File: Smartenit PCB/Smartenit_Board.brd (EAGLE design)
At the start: 54.9 x 71.8 mm, 86 parts, among them J1 2X5CONNECTOR1.27MM, Q1 QUARTZ_3.58M_2PIN, U1 SN74LVC1G3157, U2 ADE7953, U3 ESP-WROOM-32

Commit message: fixed diodes
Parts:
- D1: value (none) -> P6SMB16A; device SparkFun:SMA-DIODE -> diode:SMB
- D3: value 250mA/100V -> SS32_DIODE; device diode:DO214BA -> Smart_Charger:D0-214AB
- moved D1 72.2 mm to (-6.22, -78.3), turned to 0 degrees
- moved D3 51.8 mm to (-11.4, -68.6), turned to 0 degrees
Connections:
- net AGND: now also D3.P; no longer D3.A
- net N$18: now also D3.N; no longer D3.C
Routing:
- net N$18: track 14.6 -> 10.8 mm
- net PILOT: track 72.6 -> 69.1 mm
- net DGND: track 104.3 -> 103.6 mm
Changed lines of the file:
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@@
 <attribute name="VALUE" x="47.6154" y="-57.9006" size="0.3048" layer="27" font="vector" ratio="20" align="top-center"/>
-</element>
-<element name="D3" library="diode" library_urn="urn:adsk.eagle:library:210" package="DO214BA" package3d_urn="urn:adsk.eagle:package:43453/2" value="250mA/100V" x="39.156" y="-57.0584" smashed="yes" rot="R90">
-<attribute name="NAME" x="39.3846" y="-59.4206" size="0.6096" layer="25" font="vector" ratio="20" rot="R90" align="bottom-center"/>
 </element>
 <element name="R39" library="SparkFun-Resistors" package="0603" value="100k" x="25.76" y="-68.59" smashed="yes" rot="R180">
@@
 <attribute name="NAME" x="24.977" y="-7.841" size="1.27" layer="25"/>
 <attribute name="VALUE" x="25.231" y="-13.429" size="1.27" layer="27"/>
-</element>
-<element name="D1" library="SparkFun" package="SMA-DIODE" value="" x="13.85" y="-8.96" smashed="yes" rot="R180">
-<attribute name="NAME" x="17.152" y="-10.1284" size="0.4064" layer="25" rot="R180"/>
-<attribute name="VALUE" x="13.596" y="-10.611" size="0.4064" layer="27" rot="R180"/>
 </element>
 <element name="C2" library="SparkFun" package="0603-CAP" value="10uF/6.3V" x="39.973" y="-22.5176" smashed="yes" rot="R270">
@@
 <attribute name="VALUE" x="25.9044" y="-62.7914" size="0.8128" layer="27" rot="R270"/>
 </element>
+<element name="D3" library="Smart_Charger" package="D0-214AB" value="SS32_DIODE" x="-11.3538" y="-68.6308"/>
+<element name="D1" library="diode" library_urn="urn:adsk.eagle:library:210" package="SMB" package3d_urn="urn:adsk.eagle:package:43404/2" value="P6SMB16A" x="-6.223" y="-78.3082"/>
 </elements>
 <signals>
@@
 <signal name="N$18">
 <contactref element="U$4" pad="1"/>
-<contactref element="D3" pad="C"/>
 <contactref element="L1" pad="P$2"/>
 <contactref element="C25" pad="2"/>
-<wire x1="39.0752" y1="-58.975" x2="39.156" y2="-59.1084" width="0.6096" layer="1"/>
 <wire x1="36.3928" y1="-60.3588" x2="35.92" y2="-59.886" width="0.8128" layer="1"/>
 <wire x1="35.92" y1="-59.886" x2="35.92" y2="-58.975" width="0.8128" layer="1"/>
 <wire x1="35.92" y1="-58.975" x2="39.0752" y2="-58.975" width="0.8128" layer="1"/>
-<wire x1="39.156" y1="-59.1084" x2="41.6114" y2="-56.4388" width="0.8128" layer="1"/>
 <wire x1="41.6114" y1="-56.4388" x2="47.3516" y2="-56.4388" width="0.8128" layer="1"/>
 <wire x1="47.3516" y1="-56.4388" x2="47.6154" y2="-56.7026" width="0.8128" layer="1"/>
+<contactref element="D3" pad="N"/>
+<wire x1="35.92" y1="-59.886" x2="-4.5438" y2="-68.6308" width="0" layer="19" extent="1-1"/>
+<wire x1="41.6114" y1="-56.4388" x2="39.0752" y2="-58.975" width="0" layer="19" extent="1-1"/>
 </signal>
 <signal name="N$19">
@@
 <contactref element="R8" pad="2"/>
 <contactref element="R3" pad="2"/>
-<contactref element="D1" pad="C"/>
 <contactref element="U$3" pad="8"/>
 <wire x1="5.015" y1="-13.365" x2="4.4" y2="-13.98" width="0.6096" layer="1"/>
@@
 <wire x1="3.13" y1="-22.76" x2="3.2" y2="-22.83" width="0.4064" layer="16"/>
 <wire x1="5.015" y1="-13.365" x2="9.42" y2="-8.96" width="0.8" layer="1"/>
-<wire x1="9.42" y1="-8.96" x2="11.7" y2="-8.96" width="0.8" layer="1"/>
-<wire x1="11.7" y1="-8.96" x2="12.5906" y2="-8.0694" width="0.8" layer="1"/>
 <wire x1="12.5906" y1="-8.0694" x2="13.97" y2="-6.69" width="0.8" layer="1"/>
 <wire x1="13.97" y1="-6.69" x2="21.69" y2="-6.69" width="0.8" layer="1"/>
@@
 <wire x1="5.56" y1="-48.565" x2="5.56" y2="-53.94" width="0.4064" layer="16"/>
 <wire x1="5.56" y1="-53.94" x2="3.33" y2="-56.17" width="0.4064" layer="16"/>
+<contactref element="D1" pad="C"/>
+<wire x1="3.33" y1="-56.17" x2="-8.423" y2="-78.3082" width="0" layer="19" extent="1-1"/>
+<wire x1="12.5906" y1="-8.0694" x2="9.42" y2="-8.96" width="0" layer="19" extent="1-1"/>
 </signal>
 <signal name="LNV2">
@@
 <contactref element="C24" pad="2"/>
 <contactref element="C23" pad="1"/>
-<contactref element="D3" pad="A"/>
 <contactref element="C6" pad="1"/>
 <contactref element="U$3" pad="7"/>
@@
 <wire x1="11.1506" y1="-7.8994" x2="9.2202" y2="-7.8994" width="0.6096" layer="16"/>
 <via x="9.2202" y="-7.8994" extent="1-16" drill="0.35"/>
+<contactref element="D3" pad="P"/>
+<wire x1="5.33" y1="-56.17" x2="-11.3538" y2="-68.6308" width="0" layer="19" extent="1-1"/>
+<wire x1="8.56785625" y1="-45.40714375" x2="5.33" y2="-56.17" width="0" layer="19" extent="16-16"/>
+<wire x1="5.57" y1="-40.6820875" x2="6.28185625" y2="-43.12114375" width="0" layer="19" extent="1-1"/>
+<wire x1="7.8" y1="-34.61" x2="8.07" y2="-35.86" width="0" layer="19" extent="1-16"/>
+<wire x1="7.47" y1="-32.97" x2="7.8" y2="-34.61" width="0" layer="19" extent="1-1"/>
+<wire x1="6.05" y1="-32.38" x2="7.47" y2="-32.97" width="0" layer="19" extent="1-1"/>
+<wire x1="5.11" y1="-33.89" x2="5.11" y2="-32.93" width="0" layer="19" extent="1-1"/>
+<wire x1="7.55" y1="-8.39" x2="9.2202" y2="-7.8994" width="0" layer="19" extent="1-16"/>
+<wire x1="2.86" y1="-33.88" x2="5.11" y2="-33.89" width="0" layer="19" extent="1-1"/>
+<wire x1="2.88" y1="-32.92" x2="2.86" y2="-33.88" width="0" layer="19" extent="1-1"/>
+<wire x1="19.55" y1="-10.88" x2="16.0274" y2="-12.7762" width="0" layer="19" extent="1-16"/>
+<wire x1="21.59" y1="-11.35" x2="19.55" y2="-10.88" width="0" layer="19" extent="1-1"/>
+<wire x1="13.62" y1="-48.36" x2="10.29505625" y2="-45.40714375" width="0" layer="19" extent="1-1"/>
+<wire x1="18.09" y1="-43.5" x2="17.50343125" y2="-46.2516" width="0" layer="19" extent="1-1"/>
+<wire x1="18.791" y1="-41.744" x2="18.09" y2="-43.5" width="0" layer="19" extent="1-1"/>
+<wire x1="20.78" y1="-41.93" x2="18.791" y2="-41.744" width="0" layer="19" extent="1-1"/>
+<wire x1="22.62" y1="-41.93" x2="20.78" y2="-41.93" width="0" layer="19" extent="1-1"/>
+<wire x1="22.68" y1="-39.48" x2="22.62" y2="-41.93" width="0" layer="19" extent="1-1"/>
+<wire x1="26.92" y1="-28.915" x2="24.9936" y2="-27.2288" width="0" layer="19" extent="1-16"/>
+<wire x1="15.507" y1="-41.713" x2="18.09" y2="-43.5" width="0" layer="19" extent="1-1"/>
+<wire x1="14.4" y1="-43.41" x2="15.507" y2="-41.713" width="0" layer="19" extent="1-1"/>
+<wire x1="19.37" y1="-30.9" x2="22.6" y2="-28.32" width="0" layer="19" extent="1-16"/>
+<wire x1="17.93" y1="-31.41" x2="18.7" y2="-30.9" width="0" layer="19" extent="1-16"/>
+<wire x1="19.571" y1="-33.537" x2="18.86" y2="-31.41" width="0" layer="19" extent="1-1"/>
+<wire x1="20.542" y1="-33.537" x2="19.571" y2="-33.537" width="0" layer="19" extent="1-1"/>
+<wire x1="13.106" y1="-29.212" x2="16.19" y2="-29.21" width="0" layer="19" extent="1-1"/>
+<wire x1="34.4678" y1="-39.5224" x2="29.0068" y2="-38.6334" width="0" layer="19" extent="16-16"/>
+<wire x1="36.657" y1="-51.7376" x2="34.4678" y2="-48.0568" width="0" layer="19" extent="1-16"/>
+<wire x1="40.8104" y1="-52.6822" x2="36.657" y2="-51.7376" width="0" layer="19" extent="1-1"/>
+<wire x1="22.45" y1="-63.02" x2="24.2824" y2="-58.2422" width="0" layer="19" extent="1-1"/>
+<wire x1="28.286" y1="-10" x2="23.91" y2="-13.67" width="0" layer="19" extent="1-16"/>
+<wire x1="39.6494" y1="-29.3624" x2="37.22" y2="-34.63" width="0" layer="19" extent="1-16"/>
+<wire x1="10.08" y1="-68.76" x2="5.33" y2="-56.17" width="0" layer="19" extent="1-1"/>
 </signal>
 <signal name="DGND">
@@
 <contactref element="R35" pad="1"/>
 <contactref element="U$1" pad="1"/>
-<contactref element="D1" pad="A"/>
 <contactref element="U2" pad="4"/>
 <wire x1="13.936" y1="-41.198" x2="13.936" y2="-40.122" width="0.254" layer="1"/>
@@
 <via x="17.4752" y="-8.2042" extent="1-16" drill="0.35"/>
 <wire x1="17.4752" y1="-8.2042" x2="16.7194" y2="-8.96" width="0.4064" layer="1"/>
-<wire x1="16.7194" y1="-8.96" x2="16" y2="-8.96" width="0.4064" layer="1"/>
 <wire x1="17.4752" y1="-8.2042" x2="28.2058" y2="-8.2042" width="0.4064" layer="16"/>
 <wire x1="28.2058" y1="-8.2042" x2="33.08" y2="-3.33" width="0.4064" layer="16"/>
@@
 <wire x1="7.5438" y1="-6.8072" x2="7.5438" y2="-9.7282" width="0.4064" layer="16"/>
 <wire x1="7.5438" y1="-9.7282" x2="8.255" y2="-10.4394" width="0.4064" layer="16"/>
+<contactref element="D1" pad="A"/>
+<wire x1="20.2692" y1="-52.2224" x2="-4.023" y2="-78.3082" width="0" layer="19" extent="1-1"/>
+<wire x1="22.0894" y1="-51.3392" x2="20.2692" y2="-52.2224" width="0" layer="19" extent="1-1"/>
+<wire x1="22.8204" y1="-54.2712" x2="22.0894" y2="-51.3392" width="0" layer="19" extent="1-1"/>
+<wire x1="25.8534" y1="-54.2966" x2="22.8204" y2="-54.2712" width="0" layer="19" extent="1-1"/>
+<wire x1="24.13" y1="-48.5648" x2="22.0894" y2="-51.3392" width="0" layer="19" extent="1-1"/>
+<wire x1="25.17" y1="-40.22" x2="27.1018" y2="-45.593" width="0" layer="19" extent="1-16"/>
+<wire x1="24.6634" y1="-37.719" x2="25.17" y2="-40.22" width="0" layer="19" extent="1-1"/>
+<wire x1="44.92" y1="-43.63" x2="27.5336" y2="-45.593" width="0" layer="19" extent="1-1"/>
+<wire x1="44.92" y1="-25.63" x2="44.92" y2="-43.63" width="0" layer="19" extent="1-1"/>
+<wire x1="37.4126" y1="-19.8514" x2="39.1538" y2="-18.8468" width="0" layer="19" extent="1-1"/>
+<wire x1="46.7842" y1="-20.1786" x2="44.5516" y2="-18.8722" width="0" layer="19" extent="16-16"/>
+<wire x1="37.85" y1="-10.15" x2="43.6626" y2="-9.2202" width="0" layer="19" extent="1-1"/>
+<wire x1="37.85" y1="-6.64" x2="37.85" y2="-10.15" width="0" layer="19" extent="1-1"/>
 </signal>
 <signal name="N$30">

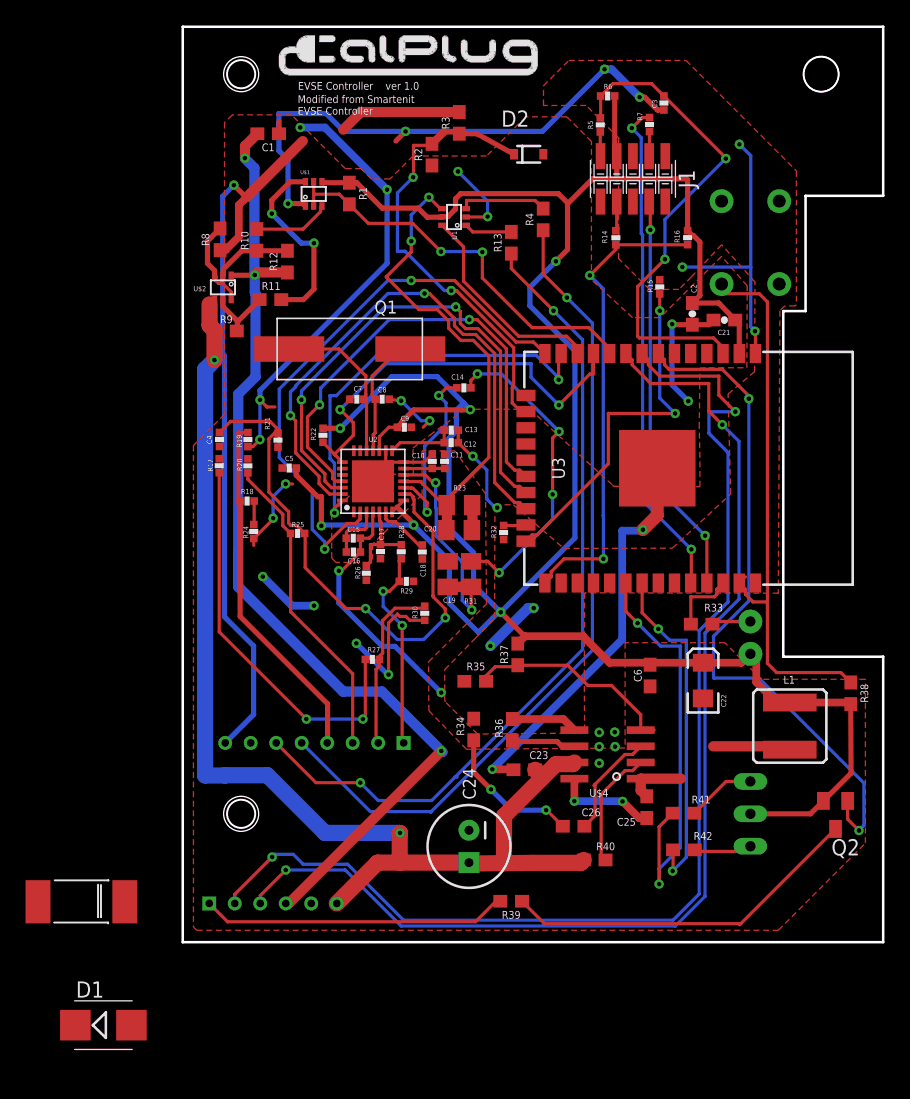
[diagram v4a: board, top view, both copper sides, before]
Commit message: New Revision with grounds connected
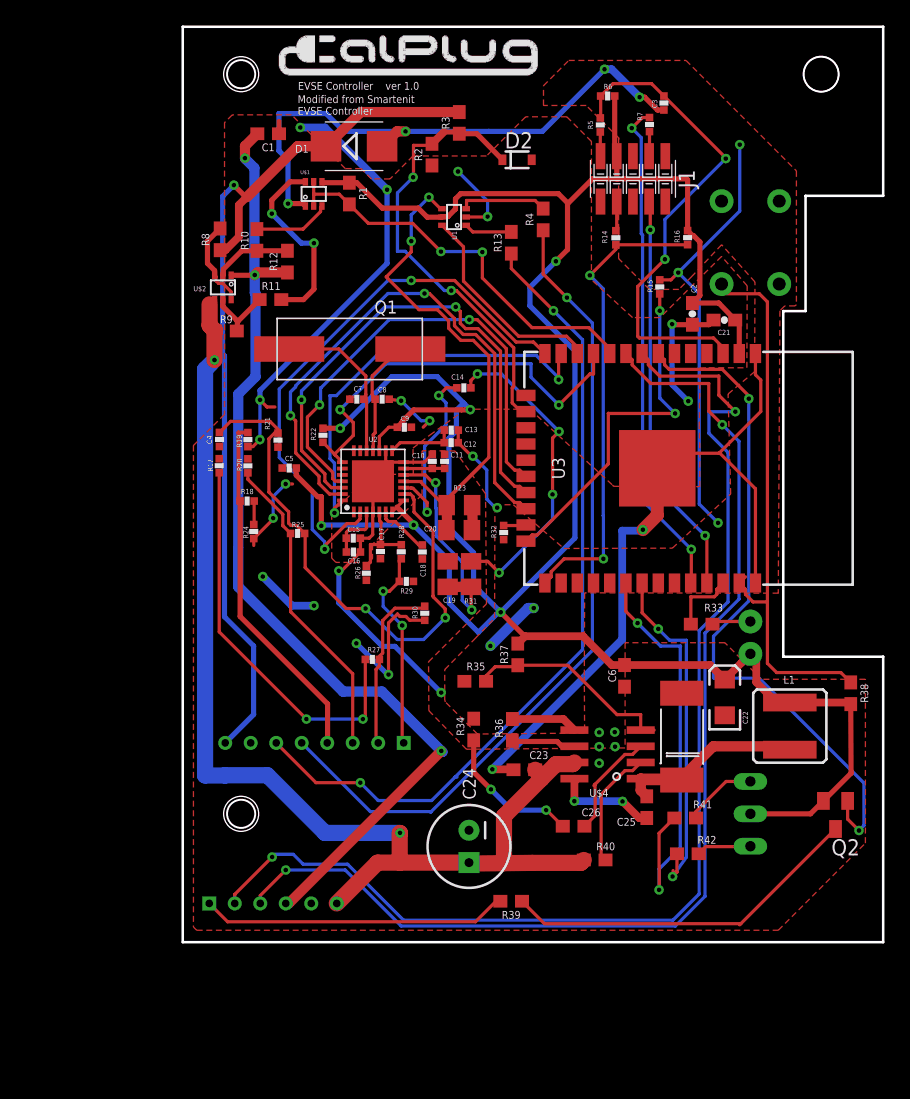
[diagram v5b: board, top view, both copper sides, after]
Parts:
- moved D1 71.7 mm to (13.4, -9.37)
- moved D3 53.1 mm to (39.1, -52.3), turned to 270 degrees
- moved C22 2.15 mm to (42.5, -52.6)
- moved C6 2.01 mm to (34.7, -50.9)
- moved D2 1.01 mm to (26.2, -10.4)
- moved R42 0.43 mm to (39.6, -64.9)
- moved R41 0.40 mm to (39.4, -62.1)
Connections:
- net AGND: now also U3.1, U3.38; no longer U2.PAD
- net DGND: now also U2.PAD; no longer U3.1, U3.38
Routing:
- net AGND: track 149.1 -> 173.0 mm
- net DGND: track 103.6 -> 120.7 mm
- net N$18: track 10.8 -> 17.8 mm
- net PILOT: track 69.1 -> 72.6 mm
- net RED_LED: track 26.9 -> 28.0 mm
- net 3.3V: track 212.8 -> 213.6 mm
- net GREEN_LED: track 33.0 -> 33.6 mm

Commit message: fixed right angles, ground planes, connectors
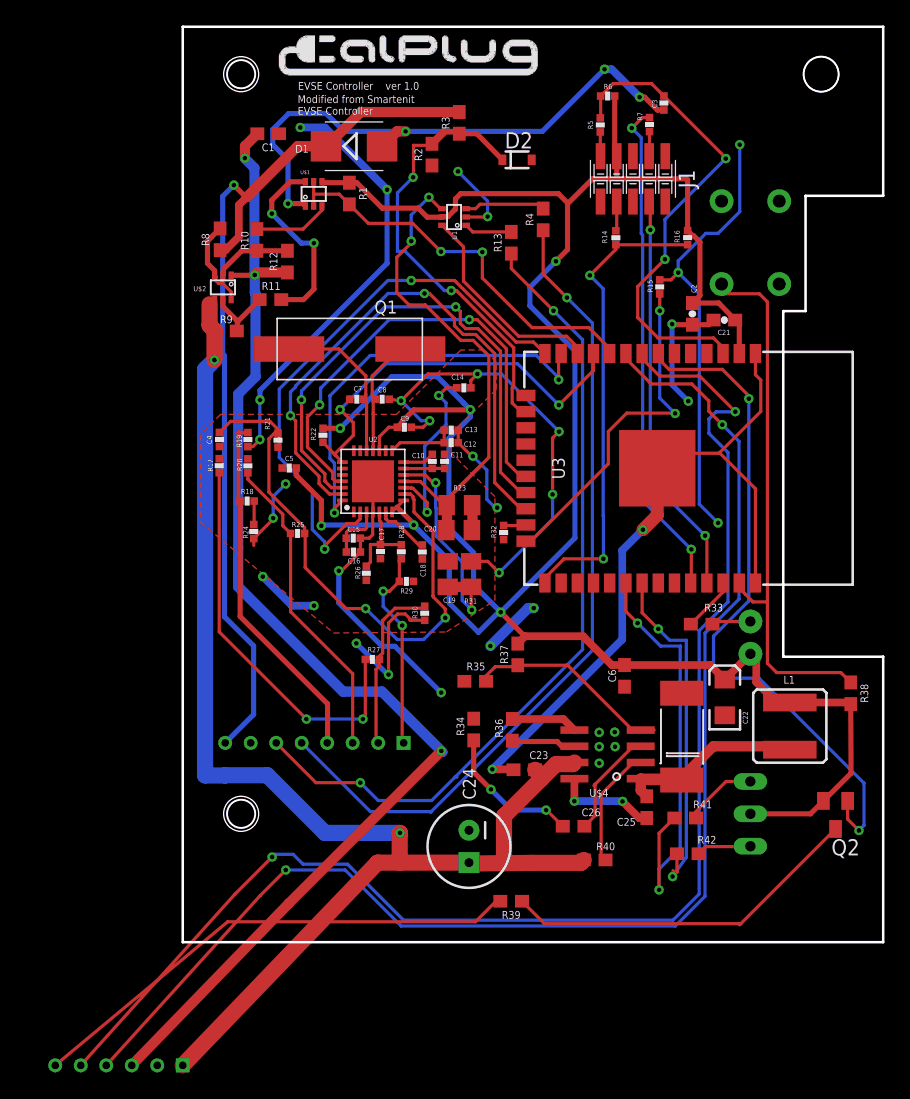
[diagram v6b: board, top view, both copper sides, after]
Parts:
- moved U$5 17.5 mm to (-10.0, -81.5)
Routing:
- net 12V: track 93.1 -> 128.1 mm
- net -12V: track 80.2 -> 97.6 mm
- net DIO12: track 89.1 -> 105.7 mm
- net DIO11: track 93.2 -> 109.3 mm
- net N$38: track 24.1 -> 39.7 mm
- net AGND: track 173.0 -> 171.2 mm
- net BLUE_LED: track 5.35 -> 4.27 mm
- net NRST: track 38.7 -> 37.9 mm
- net GPIO2: track 28.1 -> 27.2 mm
- net DIO5: track 32.7 -> 31.9 mm
- net N$3: track 39.5 -> 38.7 mm
- net N$19: track 16.8 -> 16.1 mm
- net BUTTON: track 43.9 -> 43.2 mm
- net N$55: track 6.93 -> 6.37 mm
- net DGND: track 120.7 -> 121.3 mm
- added copper zone on layer 1, net N$37
- removed copper zone on layer 1, net AGND
- removed copper zone on layer 1, net DGND

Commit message: Made Al's Revision Suggestions
-no right angles
-flipped header
-New digital ground plane (redid ground signals)
-Reorganized ADE7953 components
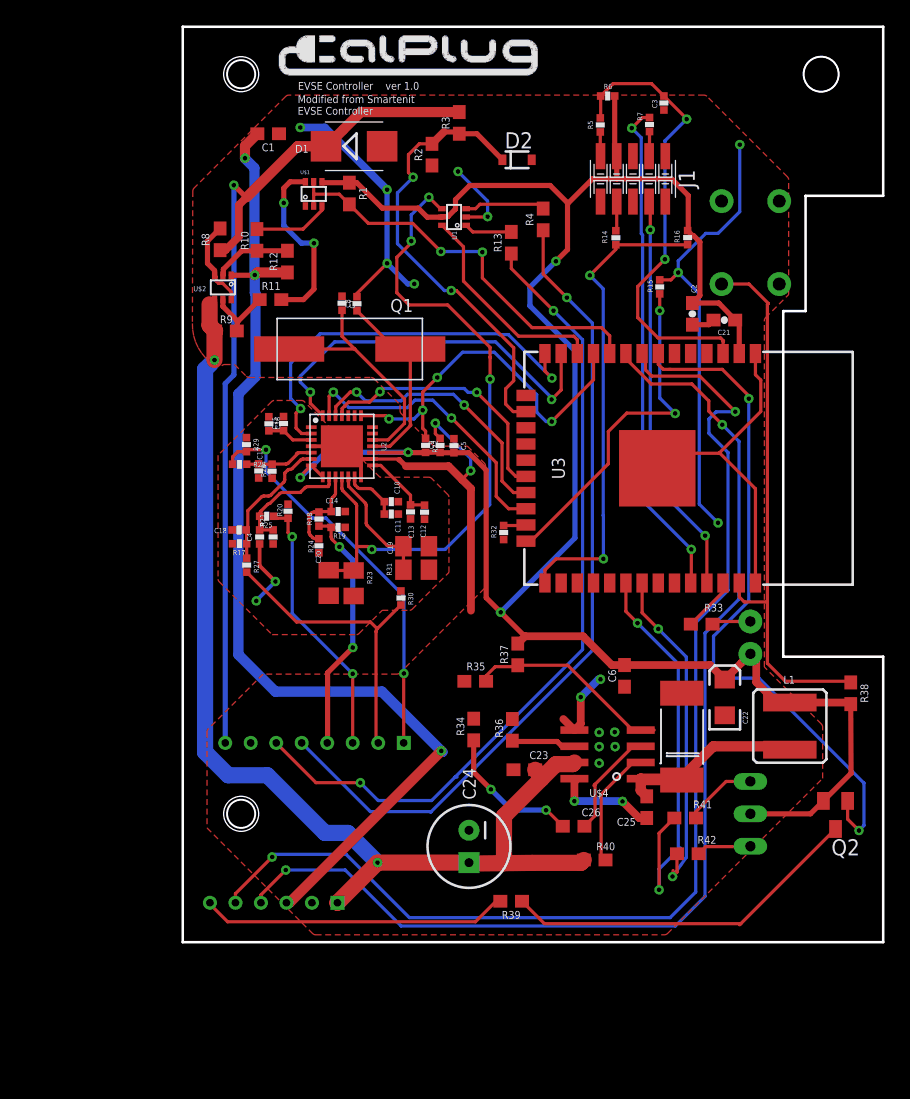
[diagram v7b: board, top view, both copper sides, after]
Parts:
- moved U$5 17.6 mm to (2.13, -68.7)
- moved R29 16.5 mm to (4.99, -32.8), turned to 270 degrees
- moved C18 14.5 mm to (4.42, -39.5), turned to 180 degrees
- moved R28 14.4 mm to (4.46, -34.3), turned to 0 degrees
- moved C14 13.8 mm to (12.2, -38.0)
- moved C5 13.0 mm to (21.3, -32.9), turned to 270 degrees
- moved R27 12.3 mm to (5.02, -42.2), turned to 90 degrees
- moved C16 12.0 mm to (6.76, -31.1), turned to 270 degrees
- moved C17 11.5 mm to (5.96, -34.8)
- moved C20 11.0 mm to (11.4, -43.6), turned to 270 degrees
- moved R26 10.9 mm to (7.01, -34.9)
- moved C15 10.5 mm to (7.90, -31.1), turned to 270 degrees
- moved R23 10.3 mm to (13.4, -43.6), turned to 270 degrees
- moved R19 9.87 mm to (12.2, -39.3), turned to 0 degrees
- moved C4 8.27 mm to (6.03, -40.0)
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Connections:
- removed net N$10: C18.1, U2.6
- removed net N$13: C14.1, U2.10
- net AGND: now also C3.1, D1.A, J1.10, R15.1, R32.1, R34.1, R35.1, R36.1, S100.1, U$1.1, U$4.5; no longer C10.2, C11.2, C14.2, C17.1, C18.2, C19.2, C20.2, C4.1, R17.2, R19.2, R20.1, R21.1, R23.2, R24.2, R26.1, R29.1, R30.2, R31.2
- net DGND: now also C10.2, C11.2, C14.2, C17.1, C18.2, C19.2, C20.2, C4.1, R17.2, R19.2, R20.1, R21.1, R23.2, R24.2, R26.1, R29.1, R30.2, R31.2; no longer C3.1, D1.A, J1.10, R15.1, R32.1, R34.1, R35.1, R36.1, S100.1, U$1.1, U$4.5
- net N$11: now also C14.1, U2.10
- net N$27: now also C18.1, U2.6
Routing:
- net DGND: track 121.3 -> 8.00 mm, vias 13 -> 2
- net AGND: track 171.2 -> 125.0 mm, vias 22 -> 13
- net 12V: track 128.1 -> 88.6 mm
- net 3.3V: track 213.2 -> 175.2 mm, vias 6 -> 4
- net N$5: track 43.1 -> 9.35 mm, vias 2 -> 0
- net SPIMOSI: track 45.3 -> 22.9 mm
- net SPIMISO: track 42.0 -> 21.6 mm
- net N$27: track 31.3 -> 11.0 mm, vias 2 -> 0
- net DIO12: track 105.7 -> 88.3 mm
- net SPISCLK: track 37.8 -> 20.6 mm
- net DIO11: track 109.3 -> 92.4 mm
- net IAP: track 16.0 -> 31.7 mm
- net N$38: track 39.7 -> 24.1 mm
- net N$13: track 15.2 -> 0.00 mm, vias 2 -> 0
- net N$3: track 38.7 -> 53.8 mm, vias 2 -> 4
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- added copper zone on layer 1, net AGND
- added copper zone on layer 1, net DGND
- removed copper zone on layer 1, net N$37
